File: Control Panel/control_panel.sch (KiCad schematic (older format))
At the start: 29 parts, among them J1 SIL16, P1 CONN_10X2, SW1 SW_PUSH, SW2 SW_PUSH, SW3 SW_PUSH, SW4 SW_PUSH, SW5 SW_PUSH, SW6 SW_PUSH, SW7 SW_PUSH, SW8 SW_PUSH, SW9 SW_PUSH

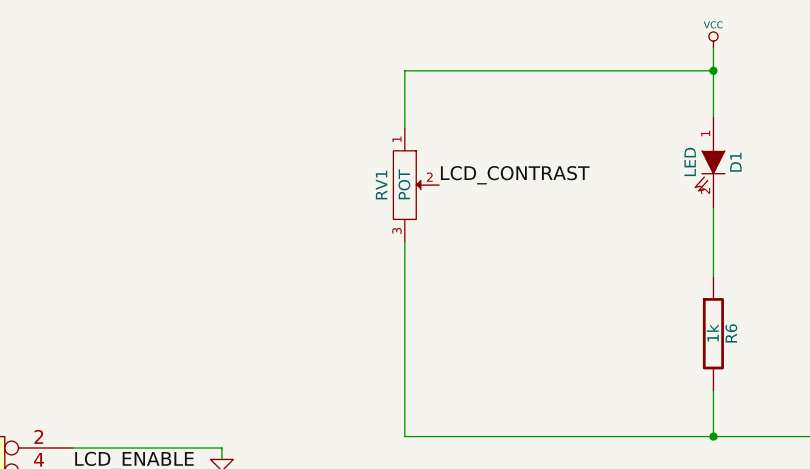
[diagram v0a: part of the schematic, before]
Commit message: Add some pdfs, PCB images
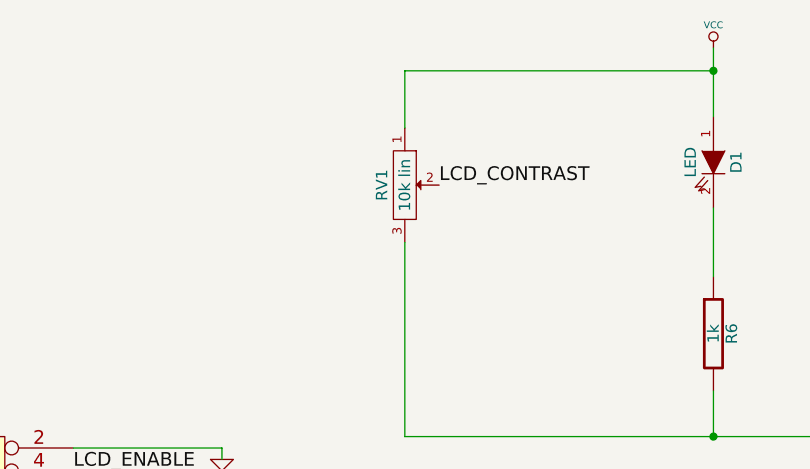
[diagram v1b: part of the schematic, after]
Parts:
- RV1: value POT -> 10k lin
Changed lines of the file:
@@
-EESchema Schematic File Version 2  date 20/05/2012 17:56:08
+EESchema Schematic File Version 2  date 22/05/2012 21:21:07
 LIBS:power
 LIBS:device
@@
 LIBS:valves
 LIBS:RMC
-EELAYER 43  0
+LIBS:control_panel-cache
+EELAYER 25  0
 EELAYER END
 $Descr A4 11700 8267
@@
 Sheet 1 1
 Title ""
-Date "20 may 2012"
+Date "22 may 2012"
 Rev ""
 Comp ""
@@
 P 3800 1500
 F 0 "RV1" H 3800 1400 50  0000 C CNN
-F 1 "POT" H 3800 1500 50  0000 C CNN
+F 1 "10k lin" H 3800 1500 50  0000 C CNN
 	1    3800 1500
 	0    1    1    0

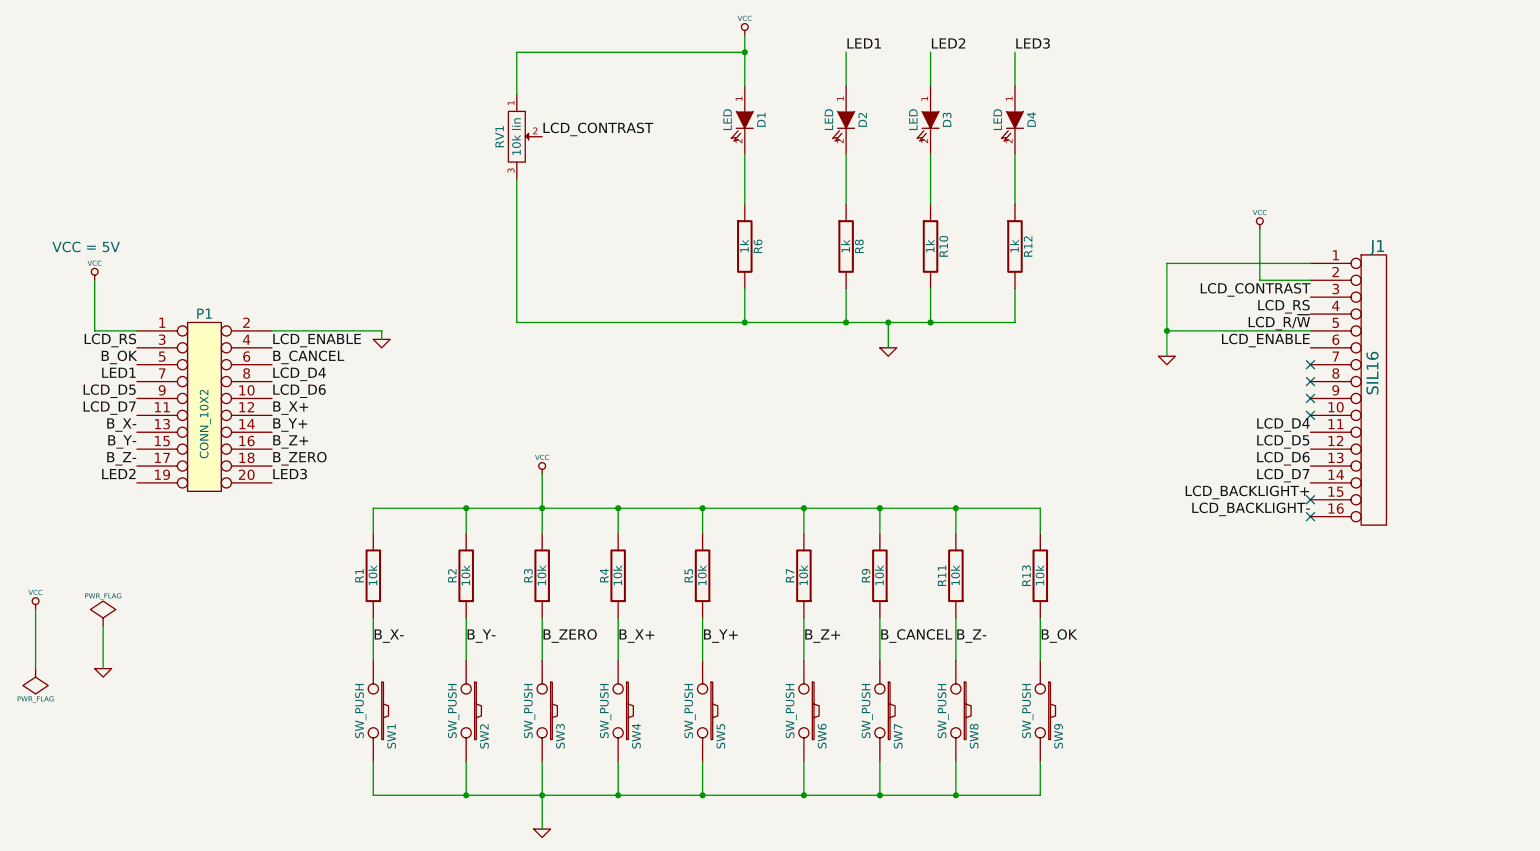
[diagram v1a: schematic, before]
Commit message: Control Panel: update to makerbot spec
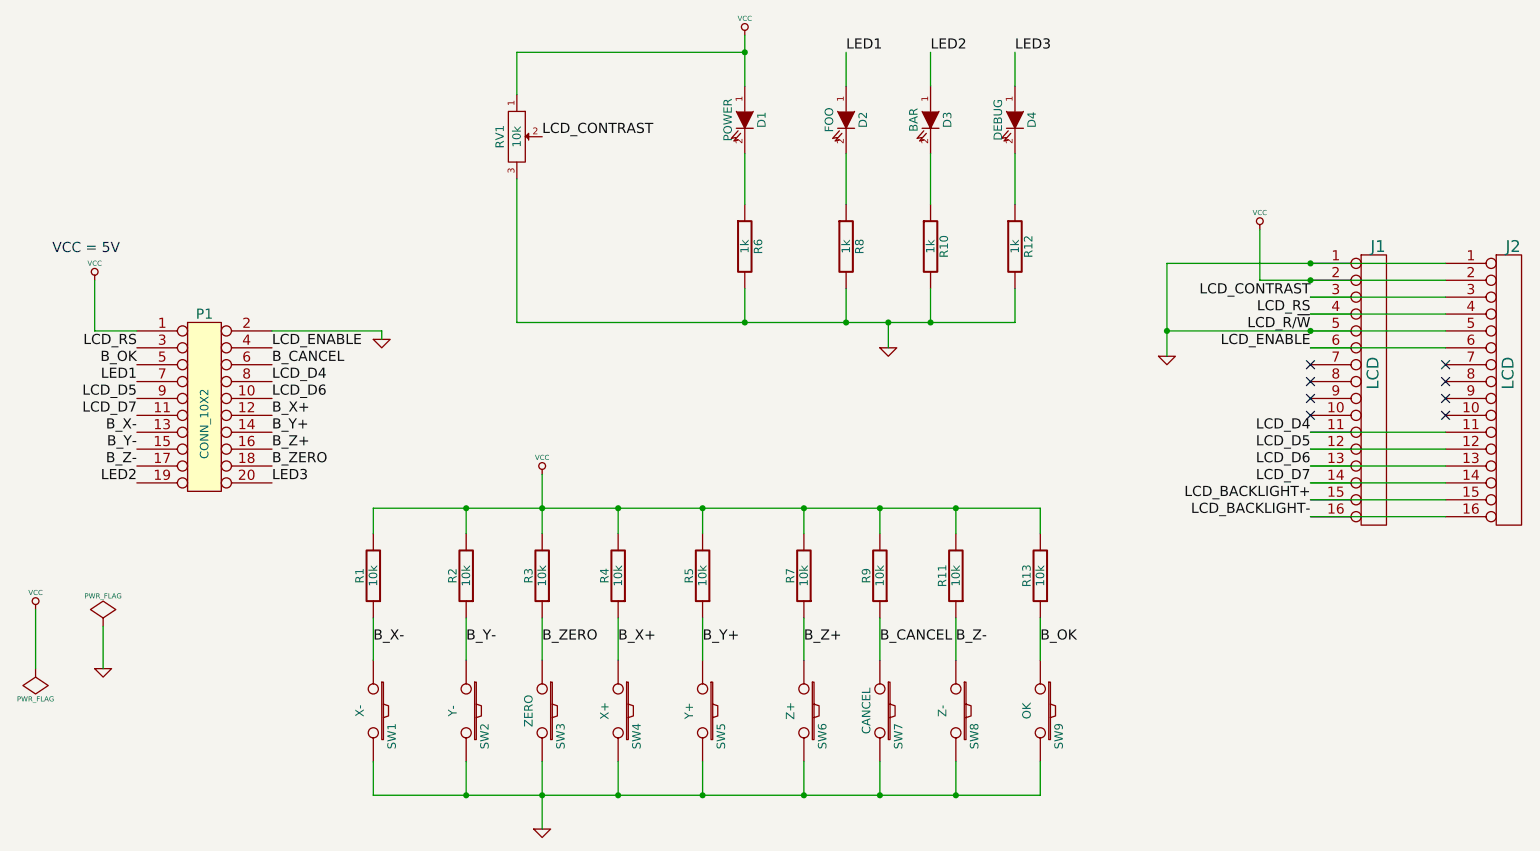
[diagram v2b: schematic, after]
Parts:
- added J2: LCD, symbol SIL16
- D1: value LED -> POWER
- D2: value LED -> FOO
- D3: value LED -> BAR
- D4: value LED -> DEBUG
- J1: value SIL16 -> LCD
- RV1: value 10k lin -> 10k
- SW1: value SW_PUSH -> X-
- SW2: value SW_PUSH -> Y-
- SW3: value SW_PUSH -> ZERO
- SW4: value SW_PUSH -> X+
- SW5: value SW_PUSH -> Y+
- SW6: value SW_PUSH -> Z+
- SW7: value SW_PUSH -> CANCEL
- SW8: value SW_PUSH -> Z-
- SW9: value SW_PUSH -> OK
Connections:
- net GND: now also J2.1, J2.5
- net LCD_BACKLIGHT+: now also J2.15
- net LCD_BACKLIGHT-: now also J2.16
- net LCD_CONTRAST: now also J2.3
- net LCD_D4: now also J2.11
- net LCD_D5: now also J2.12
- net LCD_D6: now also J2.13
- net LCD_D7: now also J2.14
- net LCD_ENABLE: now also J2.6
- net LCD_RS: now also J2.4
- net VCC: now also J2.2
- no-connect marks 6 -> 8
